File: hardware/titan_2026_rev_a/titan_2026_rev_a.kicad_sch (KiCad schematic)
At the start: 73 parts, among them J1 SEC_{OUT}, J10 Conn_02x20_Odd_Even, J2 SEC_{IN}, J3 SWD, J4 BATTERY, J5 MONITOR, J6 DHT, J7 CO_{2}, J8 WHEELS, J9 USB_B_Mini, Q1 DMG2301L, SW1 RPON, SW2 SHTDN, SW3 MCU_RST, U1 NRF24L01, U2 AP62301WU, U3 ULT-GPS, U4 STM32F103C8Tx, Y1 8MHz

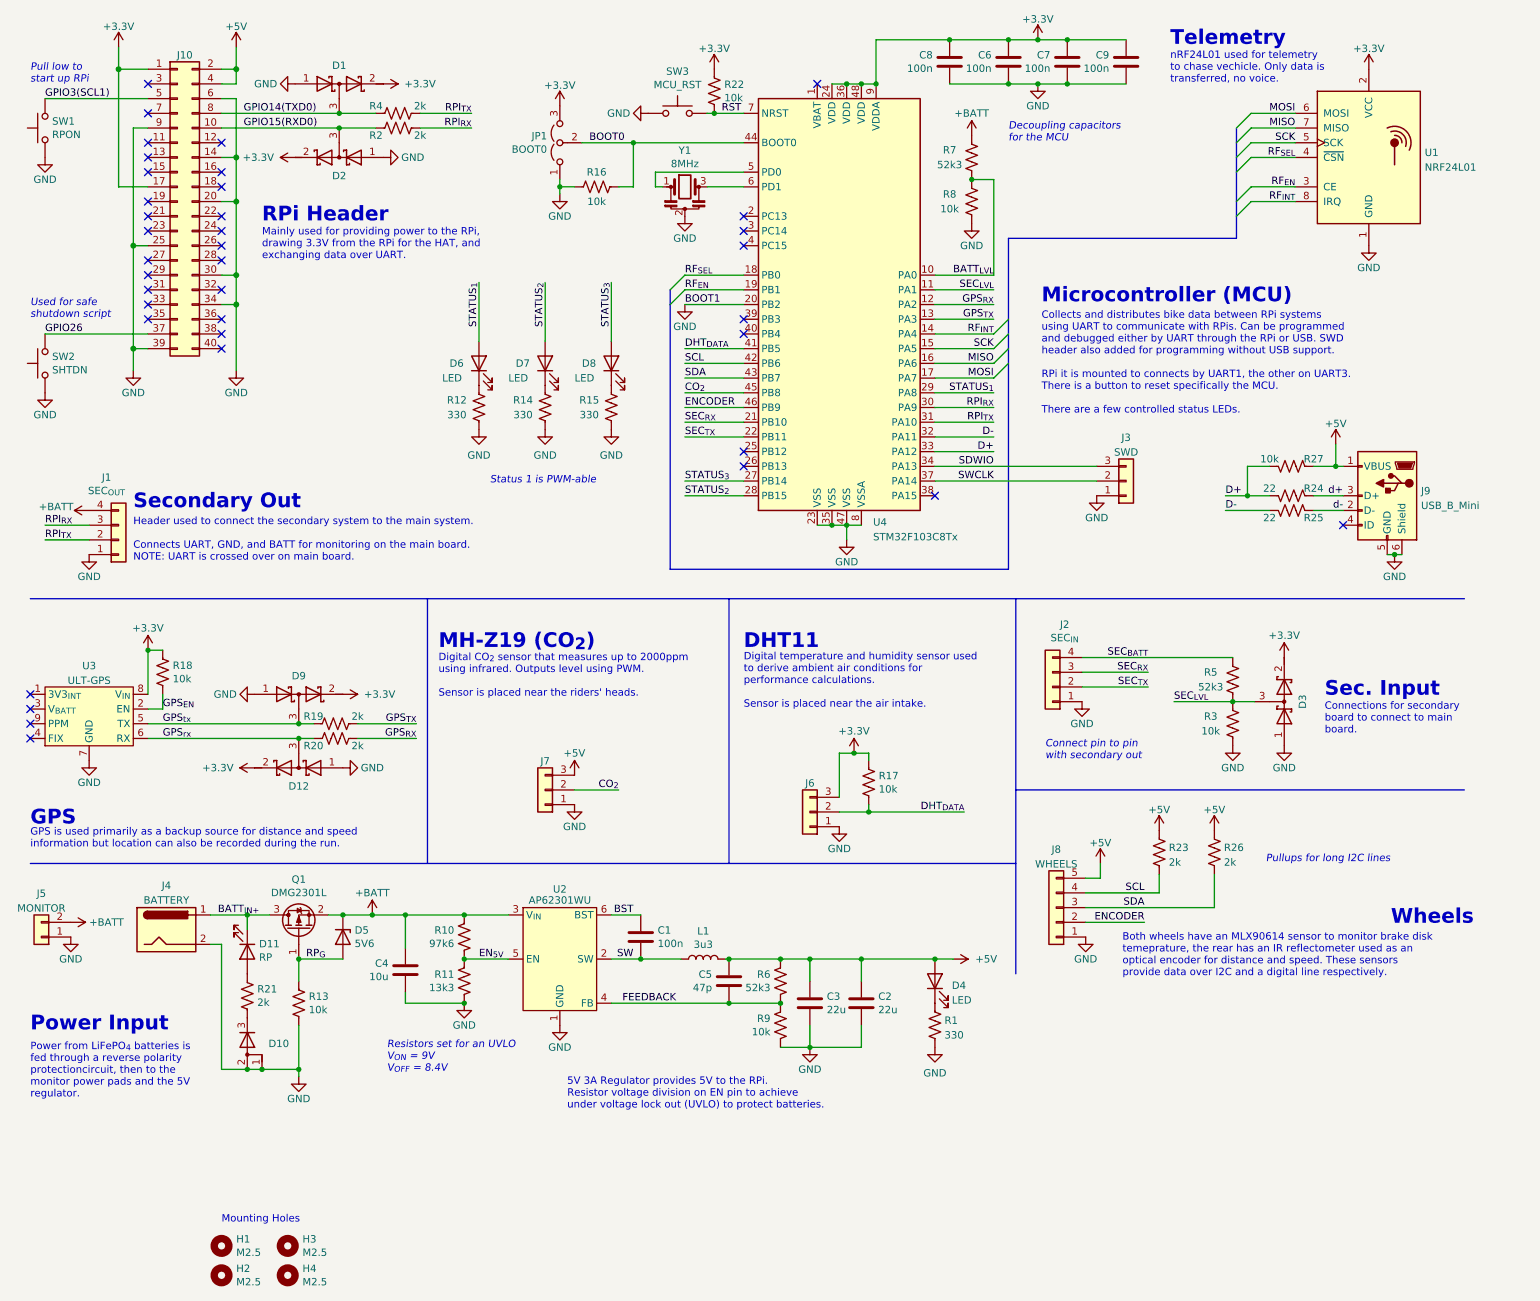
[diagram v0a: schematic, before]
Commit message: Brought KiCad projects into KiCad 10.0
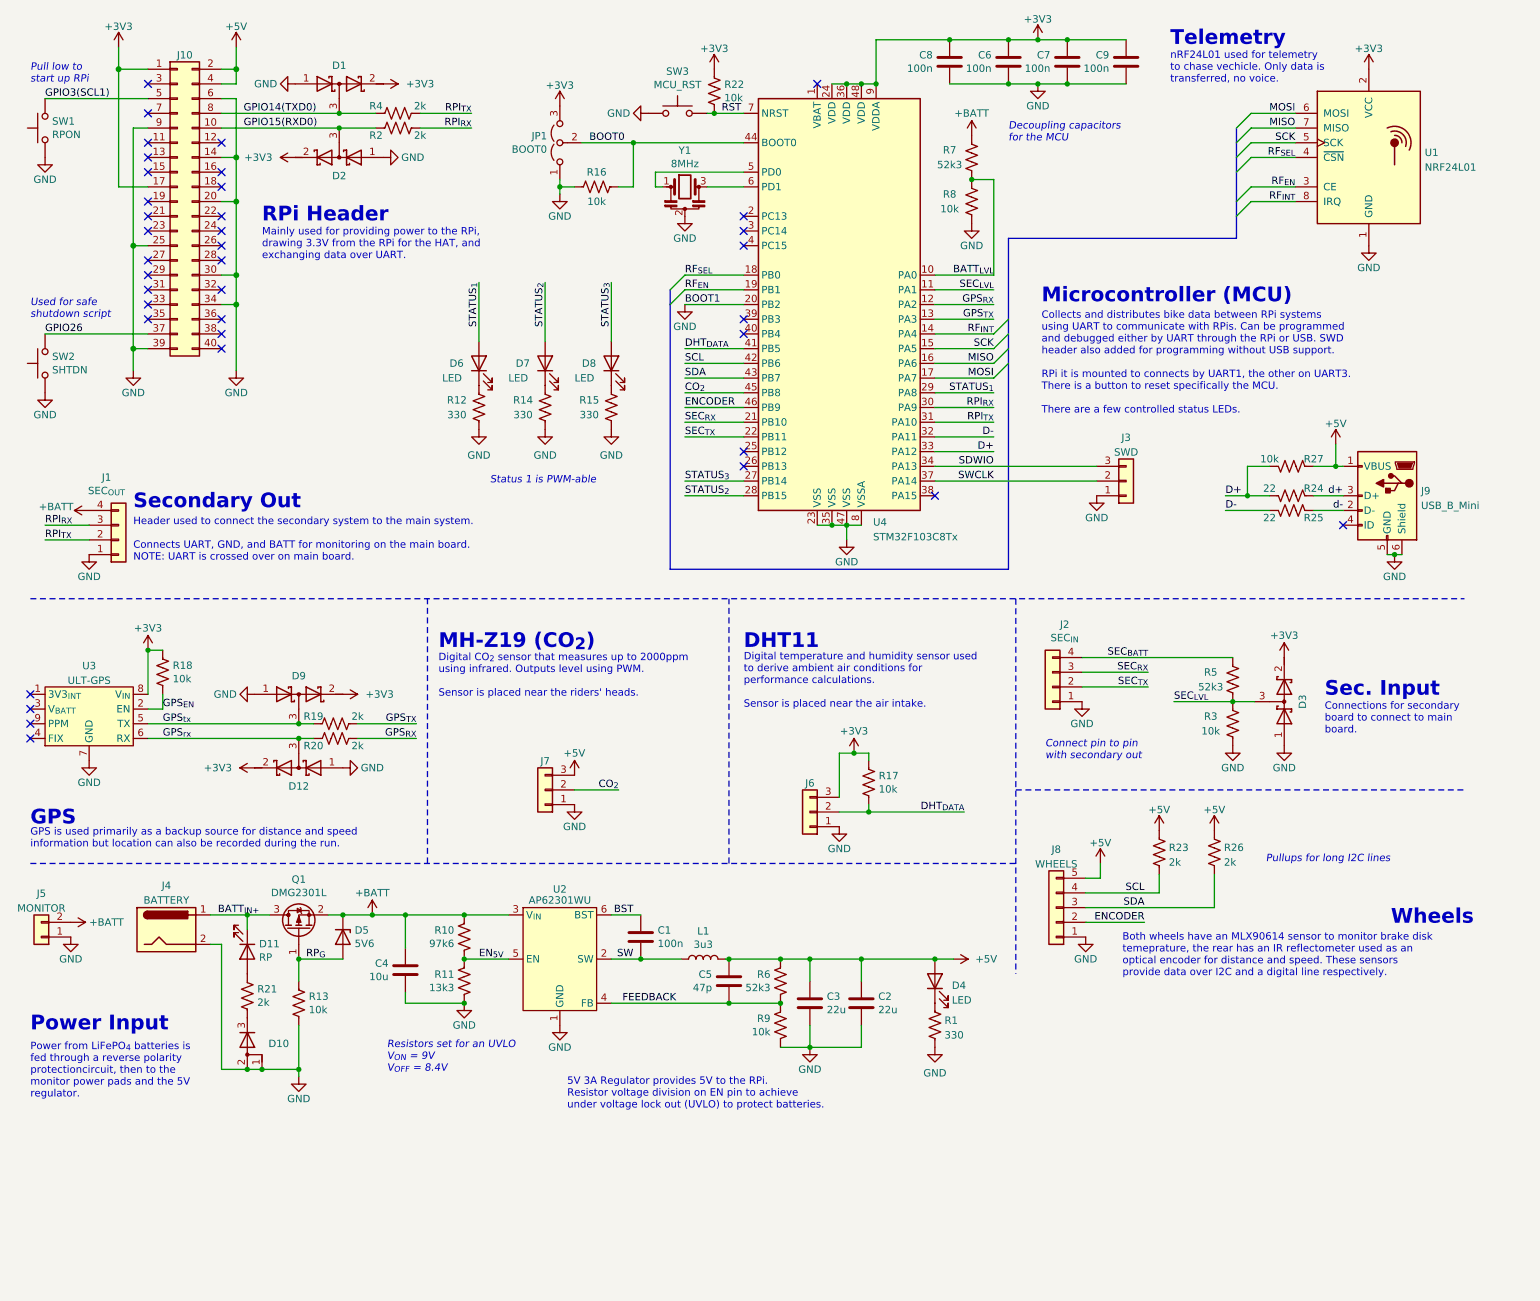
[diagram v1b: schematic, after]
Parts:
- removed H1, H2, H3, H4: M2.5, MountingHole:MountingHole_2.7mm_M2.5, symbol Mechanical:MountingHole
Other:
- note removed: "Mounting Holes"
- company: HPVDT -> Savo Bajic
- title: TITAN HAT -> TITAN HAT 2026

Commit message: Completed rev A schematics
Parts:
- removed C4: 10u, Capacitor_SMD:C_0603_1608Metric, symbol Device:C
- removed C5: 47p, Capacitor_SMD:C_0603_1608Metric, symbol Device:C
- removed D1, D12, D2, D3, D9: TBAT54S, Package_TO_SOT_SMD:SOT-23, symbol Device:D_Schottky_Dual_Series_AKC
- removed D10: BAV70, Package_TO_SOT_SMD:SOT-23, symbol Device:D_AAK
- removed D11: RP, Diode_SMD:D_0805_2012Metric, symbol Device:LED
- removed D4, D6, D7, D8: LED, LED_SMD:LED_0805_2012Metric, symbol Device:LED
- removed D5: 5V6, Diode_SMD:D_SOD-323, symbol Diode:BZX384-xxx
- removed J1: SEC_{OUT}, Connector_Molex:Molex_KK-254_AE-6410-04A_1x04_P2.54mm_Vertical, symbol Connector_Generic:Conn_01x04
- removed J2: SEC_{IN}, Connector_Molex:Molex_KK-254_AE-6410-04A_1x04_P2.54mm_Vertical, symbol Connector_Generic:Conn_01x04
- removed J3: SWD, Connector_PinHeader_2.54mm:PinHeader_1x03_P2.54mm_Vertical, symbol Connector_Generic:Conn_01x03
- removed J4: BATTERY, Connector_BarrelJack:BarrelJack_Wuerth_6941xx301002, symbol Connector:Barrel_Jack
- removed J5: MONITOR, Connector_Wire:SolderWire-1.5sqmm_1x02_P6mm_D1.7mm_OD3mm, symbol Connector_Generic:Conn_01x02
- removed J9: USB_B_Mini, 2172034-1:TE_2172034-1, symbol Connector:USB_B_Mini
- removed JP1: BOOT0, Connector_PinHeader_2.54mm:PinHeader_1x03_P2.54mm_Vertical, symbol Jumper:Jumper_3_Open
- removed L1: 3u3, Inductor_SMD:L_Taiyo-Yuden_NR-50xx, symbol Device:L
- removed Q1: DMG2301L, Package_TO_SOT_SMD:SOT-23, symbol Transistor_FET:DMG2301L
- removed R1, R12, R14, R15: 330, Resistor_SMD:R_0603_1608Metric, symbol Device:R_US
- removed R10: 97k6, Resistor_SMD:R_0603_1608Metric, symbol Device:R_US
- removed R11: 13k3, Resistor_SMD:R_0603_1608Metric, symbol Device:R_US
- removed R13, R16, R17, R18, R22, R27, R3, R8, R9: 10k, Resistor_SMD:R_0603_1608Metric, symbol Device:R_US
- removed R19, R2, R20, R21, R23, R26, R4: 2k, Resistor_SMD:R_0603_1608Metric, symbol Device:R_US
- removed R24, R25: 22, Resistor_SMD:R_0603_1608Metric, symbol Device:R_US
- removed R5, R6, R7: 52k3, Resistor_SMD:R_0603_1608Metric, symbol Device:R_US
- removed SW1: RPON, Button_Switch_THT:SW_PUSH_6mm_H4.3mm, symbol Switch:SW_Push
- removed SW2: SHTDN, Button_Switch_THT:SW_PUSH_6mm_H4.3mm, symbol Switch:SW_Push
- removed SW3: MCU_RST, Button_Switch_THT:SW_PUSH_6mm_H4.3mm, symbol Switch:SW_Push
- removed U1: NRF24L01, RF_Module:nRF24L01_Breakout, symbol RF:NRF24L01_Breakout
- removed U2: AP62301WU, Package_TO_SOT_SMD:TSOT-23-6, symbol AP62301WU:AP62301WU
- removed U3: ULT-GPS, ultimate_gps:ULT-GPS, symbol ultimate_gps:ULT-GPS
- removed U4: STM32F103C8Tx, Package_QFP:LQFP-48_7x7mm_P0.5mm, symbol MCU_ST_STM32F1:STM32F103C8Tx
- removed Y1: 8MHz, Crystal:Resonator_SMD_Murata_CSTxExxV-3Pin_3.0x1.1mm, symbol Device:Resonator
- added C8: 100n, Capacitor_SMD:C_0402_1005Metric, symbol Device:C
- added D1: RED, LED_SMD:LED_0805_2012Metric, symbol Device:LED
- added D2, D3: WHITE, LED_SMD:LED_0805_2012Metric, symbol Device:LED
- added J2: B5B-XH, Connector_JST:JST_XH_B5B-XH-A_1x05_P2.50mm_Vertical, symbol Connector_Generic:Conn_01x05
- added J6: HB-PH9-12727PB2GOB, Connector_PinHeader_1.27mm:PinHeader_2x07_P1.27mm_Vertical_SMD, symbol Connector:Conn_ST_STDC14
- added J7, J8: B7B-XH, Connector_JST:JST_XH_B7B-XH-A_1x07_P2.50mm_Vertical, symbol Connector_Generic:Conn_01x07
- added J9: USB4105-GF-A-120, Connector_USB:USB_C_Receptacle_GCT_USB4105-xx-A_16P_TopMnt_Horizontal, symbol Connector:USB_C_Receptacle_USB2.0_16P
- added R1, R2, R4: 120, Resistor_SMD:R_0402_1005Metric, symbol Device:R
- added R10, R11, R5: 5k1, Resistor_SMD:R_0402_1005Metric, symbol Device:R
- added R3: 28k, Resistor_SMD:R_0402_1005Metric, symbol Device:R
- added R6, R7, R8, R9: 2k, Resistor_SMD:R_0402_1005Metric, symbol Device:R
- added SW1, SW2: SW_SPST, titan:SW_SPST_SKPM, symbol Switch:SW_SPST
- added U1: BME280, Package_LGA:Bosch_LGA-8_2.5x2.5mm_P0.65mm_ClockwisePinNumbering, symbol Sensor:BME280
- added U2: SCD41-D-R2, Sensor:Sensirion_SCD4x-1EP_10.1x10.1mm_P1.25mm_EP4.8x4.8mm, symbol Sensor_Gas:SCD41-D-R2
- added U3: STM32F105RCT6, Package_QFP:LQFP-64_10x10mm_P0.5mm, symbol MCU_ST_STM32F1:STM32F105RCTx
- added U4: ISO1642DWR, Package_SO:SOIC-16W_7.5x10.3mm_P1.27mm, symbol Isolator:ISO1642DWR
- added U5: USBLC6-2SC6, Package_TO_SOT_SMD:SOT-23-6, symbol Power_Protection:USBLC6-2SC6
- added Y1: 8M, Crystal:Crystal_SMD_2520-4Pin_2.5x2.0mm, symbol Oscillator:ASE-xxxMHz
- C1: footprint Capacitor_SMD:C_0603_1608Metric -> Capacitor_SMD:C_0402_1005Metric; LCSC (none) -> C301928
- C2, C3: value 22u -> 100n; footprint Capacitor_SMD:C_0805_2012Metric -> Capacitor_SMD:C_0402_1005Metric; LCSC (none) -> C301928
- C4: renamed from C8; footprint Capacitor_SMD:C_0603_1608Metric -> Capacitor_SMD:C_0402_1005Metric; LCSC (none) -> C301928
- C5: renamed from C6; footprint Capacitor_SMD:C_0603_1608Metric -> Capacitor_SMD:C_0402_1005Metric; LCSC (none) -> C301928
- C6: renamed from C7; footprint Capacitor_SMD:C_0603_1608Metric -> Capacitor_SMD:C_0402_1005Metric; LCSC (none) -> C301928
- C7: renamed from C9; footprint Capacitor_SMD:C_0603_1608Metric -> Capacitor_SMD:C_0402_1005Metric; LCSC (none) -> C301928
- J1: renamed from J10; value Conn_02x20_Odd_Even -> DS1023-2*20SF11; symbol Connector_Generic:Conn_02x20_Odd_Even -> Connector:Raspberry_Pi_2_3; LCSC (none) -> C132132
- J3: renamed from J8; value WHEELS -> B5B-XH; footprint Connector_PinHeader_2.54mm:PinHeader_1x05_P2.54mm_Vertical -> Connector_JST:JST_XH_B5B-XH-A_1x05_P2.50mm_Vertical; LCSC (none) -> C157991
- J4: renamed from J7; value CO_{2} -> B3B-XH; footprint Connector_PinHeader_2.54mm:PinHeader_1x03_P2.54mm_Vertical -> Connector_JST:JST_XH_B3B-XH-A_1x03_P2.50mm_Vertical; LCSC (none) -> C144394
- J5: renamed from J6; value DHT -> B3B-XH; footprint Connector_PinHeader_2.54mm:PinHeader_1x03_P2.54mm_Vertical -> Connector_JST:JST_XH_B3B-XH-A_1x03_P2.50mm_Vertical; LCSC (none) -> C144394
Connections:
- net BST is gone; now on net GND: C1.2
- net GPIO14(TXD0) is gone; now on net RPI_{TX}: J1.8 (GPIO14/TXD)
- net GPIO15(RXD0) is gone; now on net RPI_{RX}: J1.10 (GPIO15/RXD)
- net SW is gone; now on net +3V3: C1.1
- net +3V3: now also C2.1, C3.2, J5.1 (Pin_1), C8.1, J6.3 (VCC), J8.3 (Pin_3), J8.5 (Pin_5), R3.1, R5.2, R8.1, R9.1, U1.2 (CSB), U1.5 (SDO), U1.6 (VDDIO), U1.8 (VDD), U2.19 (VDD), U2.7 (VDD), U3.1 (VBAT), U3.13 (VDDA), U3.19 (VDD), U3.32 (VDD), U3.48 (VDD), U3.64 (VDD), U4.1 (VCC1), Y1.1 (EN), Y1.4 (Vdd); no longer J1.1 (Pin_1), J1.17 (Pin_17), J5.3 (Pin_3)
- net +5V: now also J3.1 (Pin_1), J4.1 (Pin_1), J2.1 (Pin_1), R6.1, R7.1; no longer C2.1, C3.1, J3.5 (Pin_5), J4.3 (Pin_3)
- net CO_{2}: now also U3.58 (PB6)
- net DHT_{DATA}: now also R5.1, U3.56 (PB4)
- net GND: now also C3.1, J3.5 (Pin_5), J4.3 (Pin_3), J5.3 (Pin_3), C8.2, D1.1 (K), D2.1 (K), D3.1 (K), J2.5 (Pin_5), J6.11 (GNDDetect), J6.5 (GND), J6.7 (GND), J7.4 (Pin_4), J8.4 (Pin_4), J9.A1 (GND), J9.A12 (GND), J9.B1 (GND), J9.B12 (GND), J9.SH (SHIELD), R10.1, R11.1, SW1.2 (B), SW2.2 (B), U1.1 (GND), U1.7 (GND), U2.20 (GND), U2.21 (GND), U2.6 (GND), U3.12 (VSSA), U3.18 (VSS), U3.31 (VSS), U3.47 (VSS), U3.60 (BOOT0), U3.63 (VSS), U4.8 (GND1), U4.9 (GND2), U5.2 (GND), Y1.2 (GND); no longer C3.2, J3.1 (Pin_1), J4.1 (Pin_1), J5.1 (Pin_1)
- net GPS_{RX}: now also U3.16 (PA2)
- net GPS_{TX}: now also U3.17 (PA3)
- net MISO: now also U3.22 (PA6)
- net MOSI: now also U3.23 (PA7)
- net RF_{EN}: now also U3.24 (PC4)
- net RF_{INT}: now also U3.25 (PC5)
- net RPI_{RX}: now also J8.2 (Pin_2), U3.53 (PC12)
- net RPI_{TX}: now also J8.1 (Pin_1), U3.54 (PD2)
- net SCK: now also U3.21 (PA5)
- net SCL: now also J8.7 (Pin_7), R8.2, U1.4 (SCK), U2.9 (SCL), U3.29 (PB10), U4.6 (SCL1); no longer J3.4 (Pin_4)
- net SDA: now also J8.6 (Pin_6), R9.2, U1.3 (SDI), U2.10 (SDA), U3.30 (PB11), U4.3 (SDA1); no longer J3.3 (Pin_3)
- net SEC_{RX}: now also U3.51 (PC10), U4.4 (INA)
- net SEC_{TX}: now also U3.52 (PC11), U4.5 (OUTB)
- net STATUS_{1}: now also R1.2, U3.37 (PC6)
- net STATUS_{2}: now also R2.2, U3.38 (PC7)
- net STATUS_{3}: now also R4.2, U3.39 (PC8)
- net SWCLK: now also J6.6 (JCLK/SWCLK), U3.49 (PA14)
- net ENCODER renamed SCL_{WHL}
- net SCL_{WHL}: now also J2.2 (Pin_2), R6.2, U3.61 (PB8)
- net GPIO26 renamed SHUTDOWN_RPI
- net SHUTDOWN_RPI: now also SW1.1 (A)
- net GPIO3(SCL1) renamed START_RPI
- net START_RPI: now also SW2.1 (A)
- new net: J9.A5 (CC1), R10.2
- new net: D2.2 (A), R2.1
- new net: D1.2 (A), R1.1
- new net: U3.5 (PD0), Y1.3 (OUT)
- new net: J9.B5 (CC2), R11.2
- new net: D3.2 (A), R4.1
- new net +3V3_RPI: J1.1 (3V3), J1.17 (3V3)
- new net 3V3_EXT: J7.3 (Pin_3), J7.5 (Pin_5), U4.16 (VCC2)
- new net ENC_FRONT: J2.4 (Pin_4), U3.50 (PA15)
- new net ENC_REAR: J3.4 (Pin_4), U3.41 (PA8)
- new net PORT+: J9.A6 (D+), J9.B6 (D+), U5.3 (I/O2)
- new net PORT-: J9.A7 (D-), J9.B7 (D-), U5.1 (I/O1)
- new net RF_{CS}: U3.20 (PA4)
- new net RX_{ISO}: J7.6 (Pin_6), U4.13 (OUTA)
- new net SCL_{ISO}: J7.1 (Pin_1), U4.11 (SCL2)
- new net SDA_{ISO}: J7.2 (Pin_2), U4.14 (SDA2)
- new net SDA_{WHL}: J2.3 (Pin_3), J3.3 (Pin_3), R7.2, U3.62 (PB9)
- new net SWDIO: J6.4 (JTMS/SWDIO), U3.46 (PA13)
- new net SWO: J6.8 (JTDO/SWO), U3.55 (PB3)
- new net TX_{ISO}: J7.7 (Pin_7), U4.12 (INB)
- new net USB+: U3.45 (PA12), U5.4 (I/O2)
- new net USB-: U3.44 (PA11), U5.6 (I/O1)
- new net VBUS: J9.A4 (VBUS), J9.A9 (VBUS), J9.B4 (VBUS), J9.B9 (VBUS), U5.5 (VBUS)
- new net VCP_RX: J6.13 (VCP_RX), U3.43 (PA10)
- new net VCP_TX: J6.14 (VCP_TX), U3.42 (PA9)
- new net ~{RST}: J6.12 (~{RST}), R3.2, U3.7 (NRST)
- no-connect marks 38 -> 48
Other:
- added sheet Power (power.kicad_sch)
- added sheet Radio Systems (radio.kicad_sch)
- note added: "All LEDs are on PWM"
- note added: "Encoder pins must be 5V tolerant!"
- note added: "Expecting standard crossover cables hence the reversed numbering"
- note added: "I^{2}C addess is 0x77"
- note added: "I^{2}C to wheels must be 5V tolerant"
- note removed: "5V 3A Regulator provides 5V to the RPi. Resistor voltage division on EN pin to achieve under voltage lock out (UVLO) to protect batteries."
- note removed: "Collects and distributes bike data between RPi systems using UART to communicate with RPis. Can be programmed and debugged either by UART through the RPi or USB. SWD header also added for programming without USB support. RPi it is mounted to connects by UART1, the other on UART3. There is a button to reset specifically the MCU. There are a few controlled status LEDs."
- note removed: "Connect pin to pin with secondary out"
- note removed: "Decoupling capacitors for the MCU"
- note removed: "GPS"
- note removed: "GPS is used primarily as a backup source for distance and speed information but location can also be recorded during the run."
- note removed: "Power Input"
- note removed: "Power from LiFePO_{4} batteries is fed through a reverse polarity protectioncircuit, then to the monitor power pads and the 5V regulator."
- note removed: "Pullups for long I2C lines"
- note removed: "Resistors set for an UVLO V_{ON} = 9V V_{OFF} = 8.4V"
- note removed: "Status 1 is PWM-able"
- note removed: "Telemetry"
- note removed: "nRF24L01 used for telemetry to chase vechicle. Only data is transferred, no voice."
- moved on the sheet: C4, C5, C6, C7, J3, J4, J5

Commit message: Added ROLE signal and I2C address notes
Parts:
- added R22: 28k, Resistor_SMD:R_0402_1005Metric, symbol Device:R
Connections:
- net +3V3: no longer J8.3 (Pin_3)
- net GND: now also R22.2
- net ROLE: now reaches J1.15 (GPIO22)
- net ROLE: now also J8.3 (Pin_3), U3.4 (PC15), R22.1
- no-connect marks 48 -> 46
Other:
- sheet Power ports: added ADD; removed none
- note added: "I^{2}C addess is 0x62"
- note added: "I^{2}C addesses are 0x02 and 0x03"
- moved on the sheet: D1, D2, D3, R1, R2, R4

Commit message: Completed schematics for rev A
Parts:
- removed C1, C2: 100n, Capacitor_SMD:C_0402_1005Metric, symbol Device:C
- removed J2, J3: B5B-XH, Connector_JST:JST_XH_B5B-XH-A_1x05_P2.50mm_Vertical, symbol Connector_Generic:Conn_01x05
- removed J4, J5: B3B-XH, Connector_JST:JST_XH_B3B-XH-A_1x03_P2.50mm_Vertical, symbol Connector_Generic:Conn_01x03
- removed J7, J8: B7B-XH, Connector_JST:JST_XH_B7B-XH-A_1x07_P2.50mm_Vertical, symbol Connector_Generic:Conn_01x07
- removed R5: 5k1, Resistor_SMD:R_0402_1005Metric, symbol Device:R
- removed U1: BME280, Package_LGA:Bosch_LGA-8_2.5x2.5mm_P0.65mm_ClockwisePinNumbering, symbol Sensor:BME280
- removed U2: SCD41-D-R2, Sensor:Sensirion_SCD4x-1EP_10.1x10.1mm_P1.25mm_EP4.8x4.8mm, symbol Sensor_Gas:SCD41-D-R2
- removed U4: ISO1642DWR, Package_SO:SOIC-16W_7.5x10.3mm_P1.27mm, symbol Isolator:ISO1642DWR
- added JP1, JP2: SolderJumper_3_Open, Jumper:SolderJumper-3_P2.0mm_Open_TrianglePad1.0x1.5mm, symbol Jumper:SolderJumper_3_Open
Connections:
- net SCL: now also JP1.1 (A)
- net SDA: now also JP2.1 (A)
- net SHUTDOWN_RPI renamed RPI_ON
- net START_RPI renamed RPI_OFF
- new net Power/SCL: JP2.2 (C)
- new net Power/SDA: JP1.2 (C)
- new net SCL_{SEC}: JP1.3 (B)
- new net SDA_{SEC}: JP2.3 (B)
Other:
- added sheet Interboard Comms (interboard.kicad_sch)
- added sheet Sensors (sensors.kicad_sch)
- note removed: "Both wheels have an MLX90614 sensor to monitor brake disk temeprature, the rear has an IR reflectometer used as an optical encoder for distance and speed. These sensors provide data over I2C and a digital line respectively."
- note removed: "Connections for secondary board to connect to main board."
- note removed: "DHT11"
- note removed: "Digital CO_{2} sensor that measures up to 2000ppm using infrared. Outputs level using PWM. Sensor is placed near the riders' heads."
- note removed: "Digital temperature and humidity sensor used to derive ambient air conditions for performance calculations. Sensor is placed near the air intake."
- note removed: "Encoder pins must be 5V tolerant!"
- note removed: "Expecting standard crossover cables hence the reversed numbering"
- note removed: "Header used to connect the secondary system to the main system. Connects UART, GND, and BATT for monitoring on the main board. NOTE: UART is crossed over on main board."
- note removed: "I^{2}C addess is 0x62"
- note removed: "I^{2}C addess is 0x77"
- note removed: "I^{2}C addesses are 0x02 and 0x03"
- note removed: "MH-Z19 (CO_{2})"
- note removed: "Mainly used for providing power to the RPi, drawing 3.3V from the RPi for the HAT, and exchanging data over UART."
- note removed: "Microcontroller (MCU)"
- note removed: "Sec. Input"
- note removed: "Secondary Out"
- note removed: "Wheels"
- title: TITAN HAT 2026 -> TITAN HAT 2026 Core
- moved on the sheet: C3, C4, C5, C6, C7, C8, D1, D2, D3, J1, J6, R1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

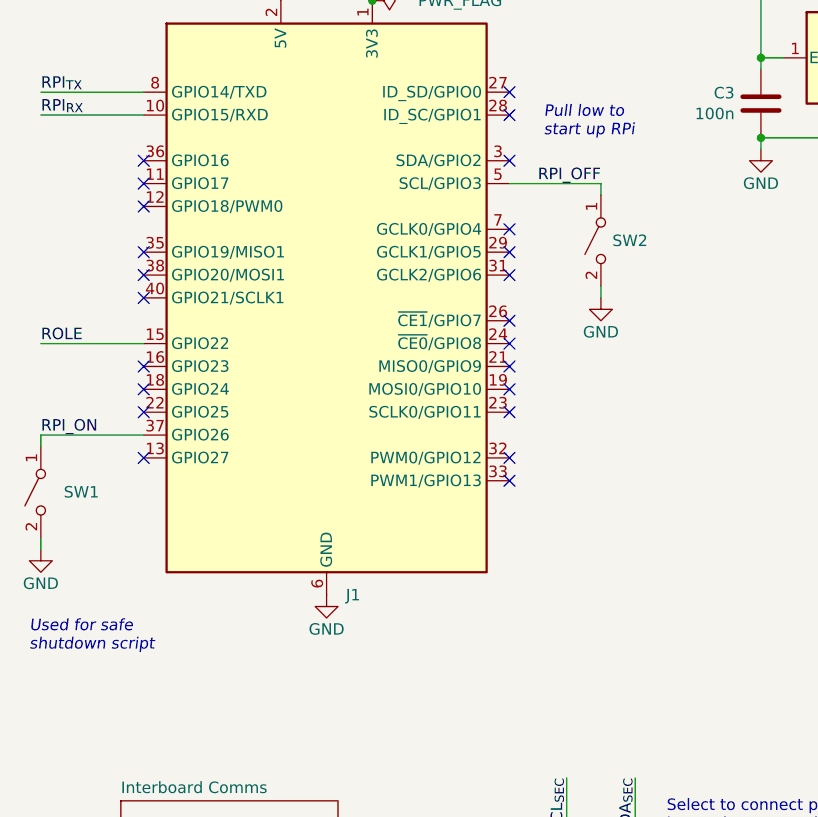
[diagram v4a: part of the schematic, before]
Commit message: Using a single switch for RPi power on/off
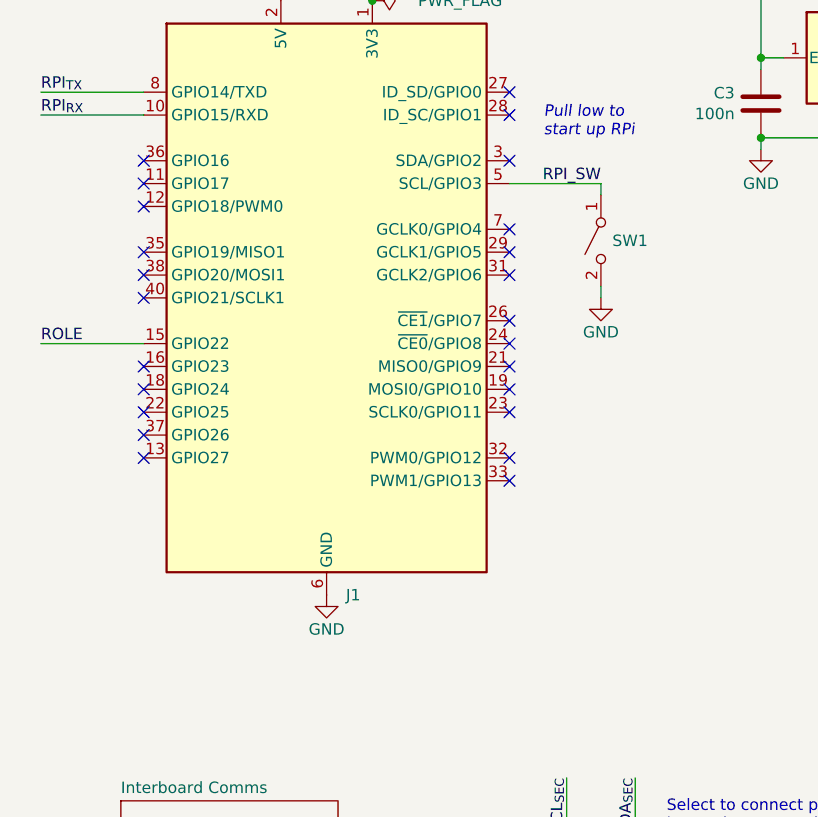
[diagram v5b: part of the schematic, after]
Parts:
- removed SW1: SW_SPST, titan:SW_SPST_SKPM, symbol Switch:SW_SPST
- renumbered SW2 to SW1
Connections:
- net RPI_OFF renamed RPI_SW
- net RPI_ON: no longer names the net of J1.37 (GPIO26)
- no-connect marks 46 -> 47
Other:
- note removed: "Used for safe shutdown script"
